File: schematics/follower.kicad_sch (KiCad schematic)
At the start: 31 parts, among them M2 Motor, M3 Motor, Q1 TLE5206_2S, Q2 TLE5206_2S, SW5 Reset, U10 PIC32MX170F256B, U5 Tape_Left, U6 Tape_Middle, U7 Tape_Right, U8 Quadrature_Encoder, U9 Quadrature_Encoder

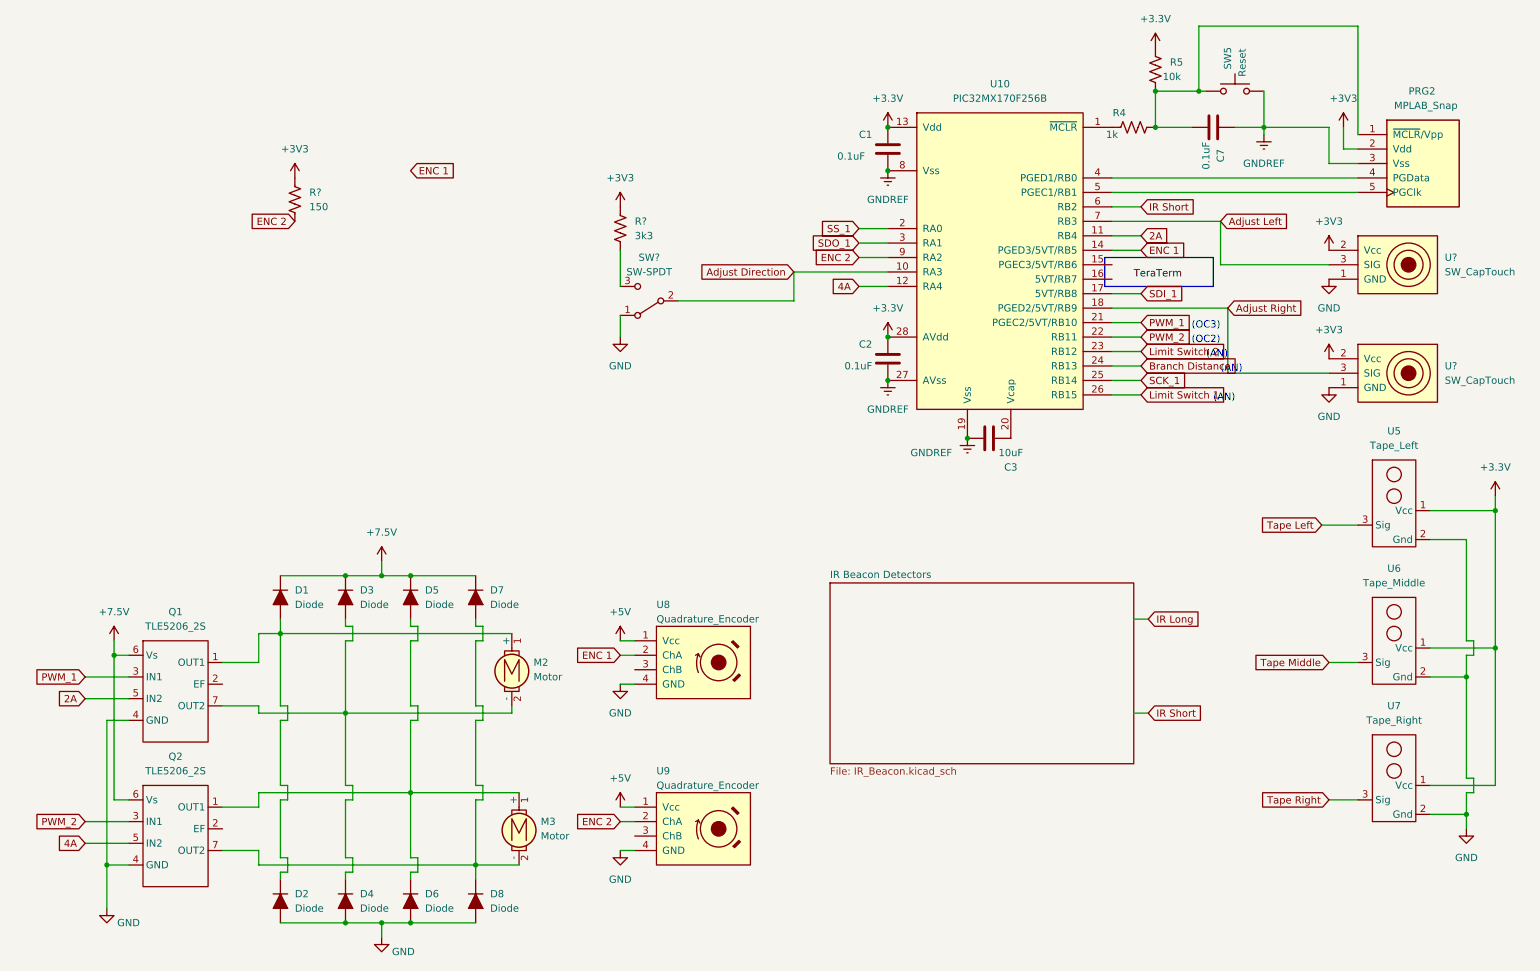
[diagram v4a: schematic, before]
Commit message: Update KiCad with new circuits, add screenshots for the website
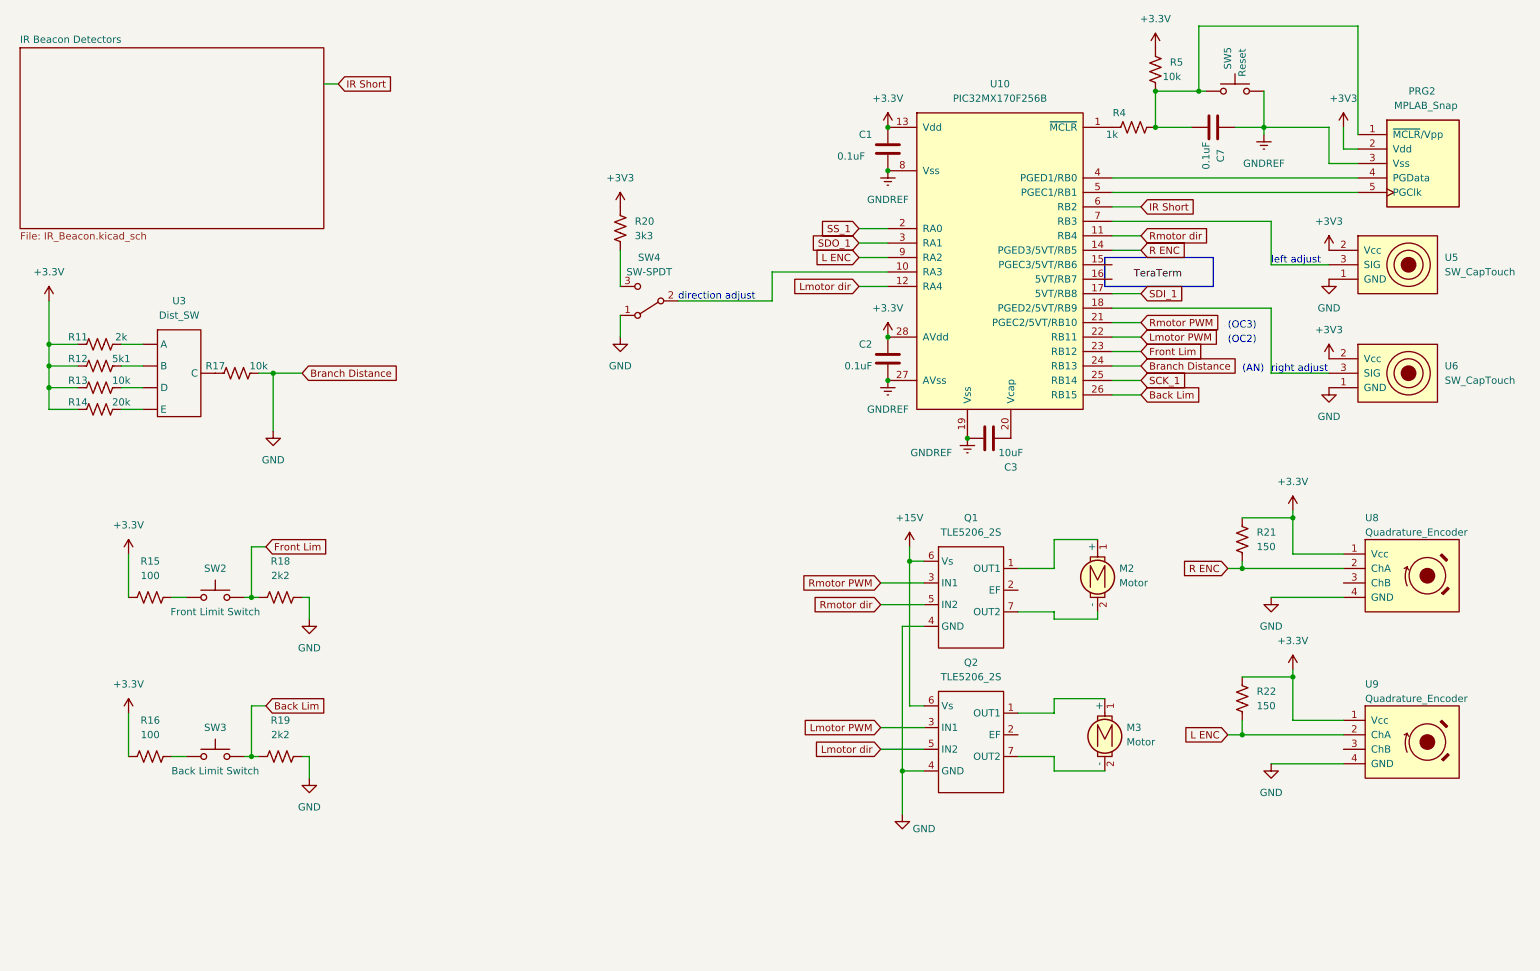
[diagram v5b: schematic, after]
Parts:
- removed D1, D2, D3, D4, D5, D6, D7, D8: Diode, symbol 218 spdl:Diode
- removed R?: 150, symbol 218 spdl:Res1
- removed U5: Tape_Left, symbol Custom_Library:Reflectance_Sensor
- removed U6: Tape_Middle, symbol Custom_Library:Reflectance_Sensor
- removed U7: Tape_Right, symbol Custom_Library:Reflectance_Sensor
- added R11: 2k, symbol 218 spdl:Res1
- added R12: 5k1, symbol 218 spdl:Res1
- added R13, R17: 10k, symbol 218 spdl:Res1
- added R14: 20k, symbol 218 spdl:Res1
- added R15, R16: 100, symbol 218 spdl:Res1
- added R18, R19: 2k2, symbol 218 spdl:Res1
- added R21, R22: 150, symbol 218 spdl:Res1
- added SW2: Front Limit Switch, symbol 218 spdl:SW-PB
- added SW3: Back Limit Switch, symbol 218 spdl:SW-PB
- added U3: Dist_SW, symbol Custom_Library:Slide_SW
- gave numbers to parts that had none: 4
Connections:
- net +5V is gone; now on net +3.3V: U8.1 (Vcc), U9.1 (Vcc)
- net Branch Distance is gone; now on net GND: U10.24 (RB13)
- net +3.3V: now also R11.1, R12.1, R13.1, R14.1, R15.1, R16.1, R21.1, R22.1
- net GND: now also R17.2, R18.2, R19.2
- net +7.5V renamed +15V
- net 2A renamed Rmotor dir
- net 4A renamed Lmotor dir
- net Adjust Direction: no longer names the net of SW4.2 (B), U10.10 (RA3)
- net Adjust Left: no longer names the net of U10.7 (RB3), U5.3 (SIG)
- net Adjust Right: no longer names the net of U10.18 (PGED2/5VT/RB9), U6.3 (SIG)
- net ENC 1 renamed R ENC
- net R ENC: now also R21.2
- net ENC 2 renamed L ENC
- net L ENC: now also R22.2
- net Limit Switch 1 renamed Back Lim
- net Back Lim: now also R19.1, SW3.2
- net Limit Switch 2 renamed Front Lim
- net Front Lim: now also R18.1, SW2.2
- net PWM_1 renamed Rmotor PWM
- net PWM_2 renamed Lmotor PWM
- new net: R13.2, U3. (E)
- new net: R11.2, U3. (E)
- new net: R17.1, U3. (E)
- new net: R14.2, U3. (E)
- new net: R12.2, U3. (E)
- new net: R15.2, SW2.1
- new net: R16.2, SW3.1
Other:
- note added: "direction adjust"
- note added: "left adjust"
- note added: "right adjust"
- moved on the sheet: M2, M3, Q1, Q2, U8, U9

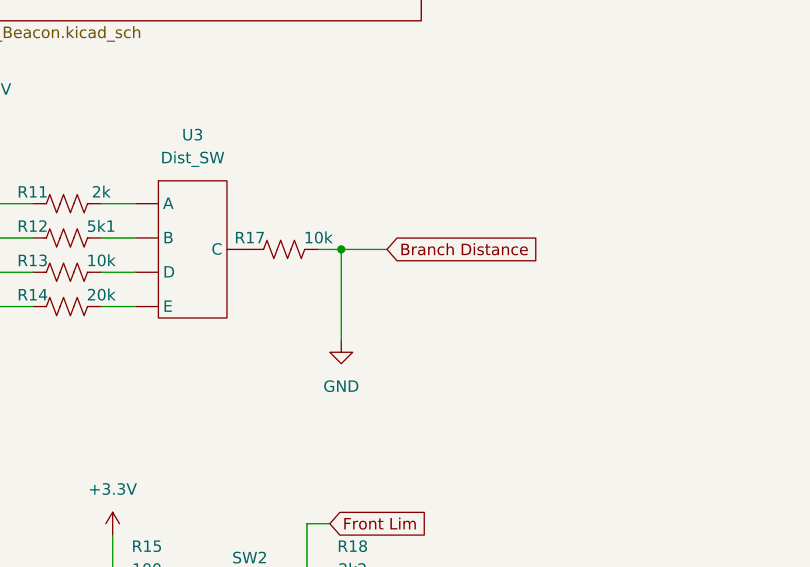
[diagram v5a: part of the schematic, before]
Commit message: Update KiCAD and CAD
* Moved input line to PIC for branch and distance switch circuits
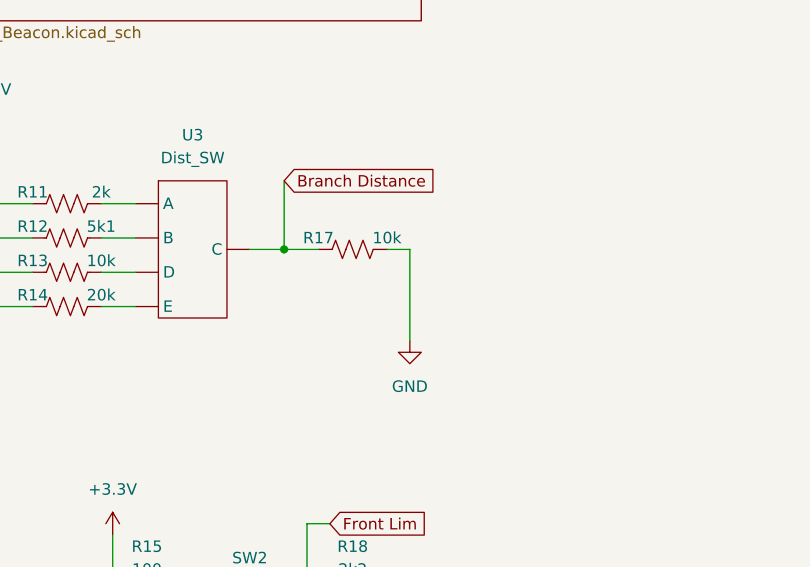
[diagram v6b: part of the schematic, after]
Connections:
- net GND: no longer U10.24 (RB13)
- net Branch Distance: now reaches R17.1, U3. (E)
- net Branch Distance: now also U10.24 (RB13)
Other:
- moved on the sheet: R17
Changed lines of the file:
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@@
   (junction (at 25.4 81.28) (diameter 0) (color 0 0 0 0)
   )
+  (junction (at 58.42 78.74) (diameter 0) (color 0 0 0 0)
+  )
   (junction (at 172.72 80.01) (diameter 0) (color 0 0 0 0)
   )
@@
   (junction (at 25.4 77.47) (diameter 0) (color 0 0 0 0)
   )
-  (junction (at 64.77 78.74) (diameter 0) (color 0 0 0 0)
-  )
   (junction (at 234.95 142.24) (diameter 0) (color 0 0 0 0)
   )
@@
     (stroke (width 0) (type default) (color 0 0 0 0))
   )
-  (wire (pts (xy 64.77 78.74) (xy 64.77 88.9))
+  (wire (pts (xy 72.39 78.74) (xy 72.39 88.9))
     (stroke (width 0) (type default) (color 0 0 0 0))
   )
@@
     (stroke (width 0) (type default) (color 0 0 0 0))
   )
-  (wire (pts (xy 64.77 78.74) (xy 69.85 78.74))
-    (stroke (width 0) (type default) (color 0 0 0 0))
-  )
   (wire (pts (xy 212.09 67.31) (xy 240.03 67.31))
     (stroke (width 0) (type default) (color 0 0 0 0))
   )
+  (wire (pts (xy 58.42 71.12) (xy 58.42 78.74))
+    (stroke (width 0) (type default) (color 0 0 0 0))
+  )
   (wire (pts (xy 179.07 123.19) (xy 175.26 123.19))
     (stroke (width 0) (type default) (color 0 0 0 0))
@@
     (stroke (width 0) (type default) (color 0 0 0 0))
   )
+  (wire (pts (xy 58.42 78.74) (xy 54.61 78.74))
+    (stroke (width 0) (type default) (color 0 0 0 0))
+  )
   (wire (pts (xy 201.93 146.05) (xy 201.93 148.59))
     (stroke (width 0) (type default) (color 0 0 0 0))
@@
     (stroke (width 0) (type default) (color 0 0 0 0))
   )
+  (wire (pts (xy 62.23 78.74) (xy 58.42 78.74))
+    (stroke (width 0) (type default) (color 0 0 0 0))
+  )
   (wire (pts (xy 179.07 137.16) (xy 176.53 137.16))
     (stroke (width 0) (type default) (color 0 0 0 0))
   )
-  (wire (pts (xy 62.23 78.74) (xy 64.77 78.74))
+  (wire (pts (xy 69.85 78.74) (xy 72.39 78.74))
     (stroke (width 0) (type default) (color 0 0 0 0))
   )
@@
     )
   )
-  (global_label "Branch Distance" (shape input) (at 69.85 78.74 0) (fields_autoplaced)
+  (global_label "Branch Distance" (shape input) (at 58.42 71.12 0) (fields_autoplaced)
     (effects (font (size 1.27 1.27)) (justify left))
-    (property "Intersheet References" "${INTERSHEET_REFS}" (id 0) (at 87.9264 78.6606 0)
+    (property "Intersheet References" "${INTERSHEET_REFS}" (id 0) (at 76.4964 71.0406 0)
       (effects (font (size 1.27 1.27)) (justify left) hide)
     )
@@
     (pin "3")
   )
-  (symbol (lib_id "218 spdl:Res1") (at 58.42 78.74 90) (unit 1)
-    (in_bom yes) (on_board yes)
-    (property "Reference" "R17" (id 0) (at 54.61 77.47 90))
-    (property "Value" "10k" (id 1) (at 62.23 77.47 90))
-    (property "Footprint" "" (id 2) (at 58.674 77.724 90)
-      (effects (font (size 1.27 1.27)) hide)
-    )
-    (property "Datasheet" "" (id 3) (at 58.42 78.74 0)
+  (symbol (lib_id "218 spdl:Res1") (at 66.04 78.74 90) (unit 1)
+    (in_bom yes) (on_board yes)
+    (property "Reference" "R17" (id 0) (at 62.23 77.47 90))
+    (property "Value" "10k" (id 1) (at 69.85 77.47 90))
+    (property "Footprint" "" (id 2) (at 66.294 77.724 90)
+      (effects (font (size 1.27 1.27)) hide)
+    )
+    (property "Datasheet" "" (id 3) (at 66.04 78.74 0)
       (effects (font (size 1.27 1.27)) hide)
     )
@@
     (pin "1")
   )
-  (symbol (lib_id "power:GND") (at 64.77 88.9 0) (unit 1)
-    (in_bom yes) (on_board yes) (fields_autoplaced)
-    (property "Reference" "#PWR024" (id 0) (at 64.77 95.25 0)
-      (effects (font (size 1.27 1.27)) hide)
-    )
-    (property "Value" "GND" (id 1) (at 64.77 93.98 0))
-    (property "Footprint" "" (id 2) (at 64.77 88.9 0)
-      (effects (font (size 1.27 1.27)) hide)
-    )
-    (property "Datasheet" "" (id 3) (at 64.77 88.9 0)
-      (effects (font (size 1.27 1.27)) hide)
-    )
+  (symbol (lib_id "power:GND") (at 72.39 88.9 0) (unit 1)
+    (in_bom yes) (on_board yes) (fields_autoplaced)
+    (property "Reference" "#PWR024" (id 0) (at 72.39 95.25 0)
+      (effects (font (size 1.27 1.27)) hide)
+    )
+    (property "Value" "GND" (id 1) (at 72.39 93.98 0))
+    (property "Footprint" "" (id 2) (at 72.39 88.9 0)
+      (effects (font (size 1.27 1.27)) hide)
+    )
+    (property "Datasheet" "" (id 3) (at 72.39 88.9 0)
+      (effects (font (size 1.27 1.27)) hide)
+    )
